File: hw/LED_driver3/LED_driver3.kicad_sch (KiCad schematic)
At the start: 100 parts, among them J1 LED_EN, J10 RJ45_Shielded, J2 I2C, J3 PROG, J4 GPIO, J5 POWER, J6 1WIRE1, J7 1WIRE2, J8 LED, J9 RJ45_Shielded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

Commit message: Routed.
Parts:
- removed TP1, TP2, TP3, TP4: TestPoint, TestPoint:TestPoint_THTPad_D2.0mm_Drill1.0mm, symbol Connector:TestPoint
- added C41: DNP, Capacitor_SMD:C_0603_1608Metric, symbol Device:C
- added R44: 0, Resistor_SMD:R_0603_1608Metric, symbol Device:R
- J5: footprint Connector_Phoenix_MSTB:PhoenixContact_MSTBA_2,5_2-G-5,08_1x02_P5.08mm_Horizontal -> Connector_Phoenix_MSTB:PhoenixContact_MSTB_2,5_2-GF-5,08_1x02_P5.08mm_Horizontal_ThreadedFlange
- R34: value 0.004R -> 6m; LCSC (none) -> C728340
- U5: value INA180 -> INA180A2; LCSC (none) -> C192764
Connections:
- net +3.3V is gone; now on net +3V3: C12.1, C13.1, C16.1, R10.1, U2.4 (VBAT), U2.6 (VDD)
- net SWCLK/BOOT0 is gone; now on net SWCLK: U2.36 (PA14)
- net 12V_SENSE: now also U2.12 (PA1); no longer U2.11 (PA0)
- net CUR_SENSE: now also C41.1, R44.2; no longer U5.1
- net GND: now also C38.2, C39.2, C40.2, C41.2
- net LED_COM: no longer C38.2, C39.2, C40.2
- net O1_SW: now also U2.19 (PB0); no longer U2.17 (PA6)
- net O3_SW: now also U2.17 (PA6); no longer U2.19 (PB0)
- net VCC_SENSE: now also U2.11 (PA0); no longer U2.12 (PA1)
- new net: R44.1, U5.1
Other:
- note added: "TODO: RC článek na sense"

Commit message: Silkscreen finished, bugfixes.
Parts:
- added R45, R46: 330R, Resistor_SMD:R_0603_1608Metric, symbol Device:R
- added R47, R48: 1k5, Resistor_SMD:R_0603_1608Metric, symbol Device:R
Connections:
- net +3V3: now also J2.3 (Pin_3), R47.2, R48.2; no longer J2.4 (Pin_4)
- net 1WIRE: now also U2.30 (PC6)
- net GND: now also J2.4 (Pin_4); no longer J2.3 (Pin_3)
- net SCL: now also R47.1; no longer R12.1, U1.6 (SCL)
- net SDA: now also R48.1; no longer R11.1, U1.5 (SDA)
- net at U2.25 (PB13): no longer R18.1
- net at U2.26 (PB14): now also R18.1; no longer R19.1
- net at U2.27 (PB15): now also R19.1; no longer R20.1
- net at U2.28 (PA8): now also R20.1; no longer R14.1
- net at U2.29 (PA9/NC): now also R14.1
- net at U2.33 (PA11/PA9): now also R45.1
- net at U2.34 (PA12/PA10): now also R46.1
- new net SCL2: R12.1, R45.2, U1.6 (SCL)
- new net SDA2: R11.1, R46.2, U1.5 (SDA)
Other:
- moved on the sheet: R14, R18, R19, R20

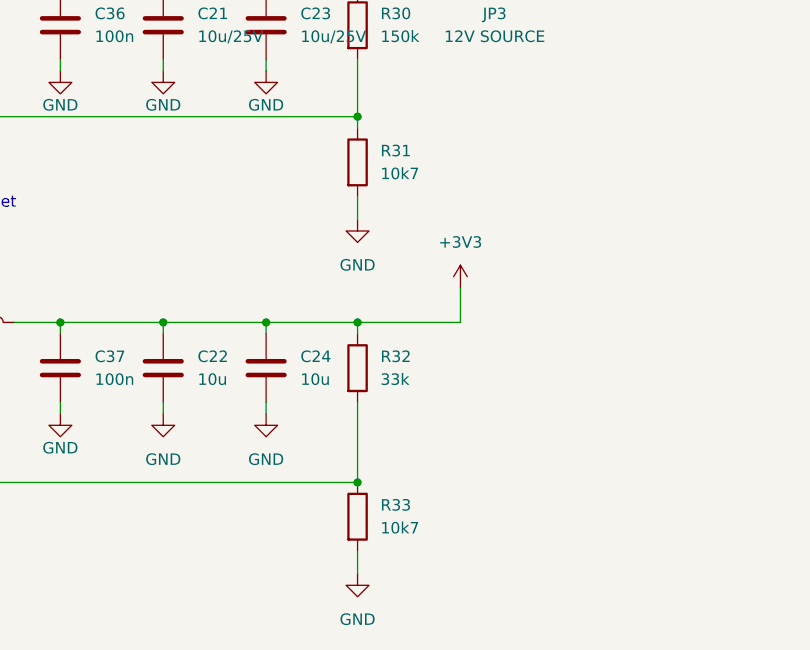
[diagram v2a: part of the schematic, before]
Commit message: Added LCSC numbers.
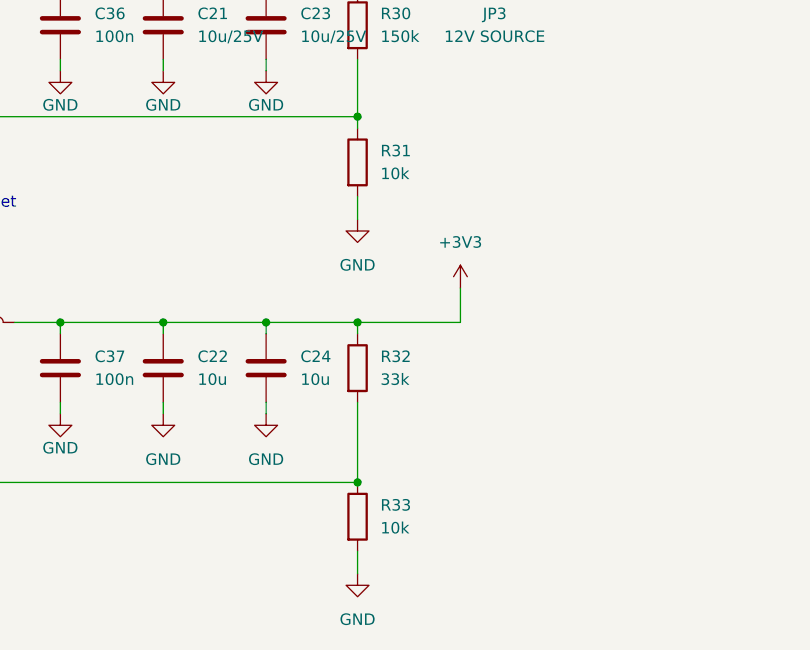
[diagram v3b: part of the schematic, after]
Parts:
- D1: LCSC C72043 -> C2286
- D2, D3, D4, D5, J8: LCSC (none) -> C2286
- R30: LCSC (none) -> C22807
- R31, R33: value 10k7 -> 10k; LCSC (none) -> C25804
- R32: LCSC (none) -> C4216
- R34: LCSC C728340 -> C728340
- R44: LCSC (none) -> C21189
- U1, U5: JLCPCB_CORRECTION (none) -> 0;0;270
- U3, U4: JLCPCB_CORRECTION (none) -> 0;0;270; LCSC (none) -> C5123972
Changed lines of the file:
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@@
 			)
 		)
+		(property "LCSC" "C5123972"
+			(at 193.04 217.17 0)
+			(effects
+				(font
+					(size 1.27 1.27)
+				)
+				(hide yes)
+			)
+		)
+		(property "JLCPCB_CORRECTION" "0;0;270"
+			(at 193.04 217.17 0)
+			(effects
+				(font
+					(size 1.27 1.27)
+				)
+				(hide yes)
+			)
+		)
 		(pin "4"
 		)
@@
 			)
 		)
+		(property "LCSC" "C2286"
+			(at 66.04 114.3 0)
+			(effects
+				(font
+					(size 1.27 1.27)
+				)
+				(hide yes)
+			)
+		)
 		(pin "1"
 		)
@@
 			)
 		)
-		(property "Value" "10k7"
+		(property "Value" "10k"
 			(at 267.97 275.5899 0)
 			(effects
@@
 			)
 		)
+		(property "LCSC" "C25804"
+			(at 265.43 274.32 0)
+			(effects
+				(font
+					(size 1.27 1.27)
+				)
+				(hide yes)
+			)
+		)
 		(pin "1"
 		)
@@
 			)
 		)
+		(property "LCSC" "C2286"
+			(at 45.72 114.3 0)
+			(effects
+				(font
+					(size 1.27 1.27)
+				)
+				(hide yes)
+			)
+		)
 		(pin "1"
 		)
@@
 			)
 		)
+		(property "LCSC" "C21189"
+			(at 354.33 110.49 0)
+			(effects
+				(font
+					(size 1.27 1.27)
+				)
+				(hide yes)
+			)
+		)
 		(pin "1"
 		)
@@
 			)
 		)
-		(property "LCSC" "C72043"
+		(property "LCSC" "C2286"
 			(at 26.67 114.3 90)
 			(effects
@@
 			)
 		)
-		(property "LCSC" "    C728340"
+		(property "LCSC" "C728340"
 			(at 314.96 110.49 0)
 			(effects
@@
 			)
 		)
+		(property "LCSC" "C5123972"
+			(at 193.04 255.27 0)
+			(effects
+				(font
+					(size 1.27 1.27)
+				)
+				(hide yes)
+			)
+		)
+		(property "JLCPCB_CORRECTION" "0;0;270"
+			(at 193.04 255.27 0)
+			(effects
+				(font
+					(size 1.27 1.27)
+				)
+				(hide yes)
+			)
+		)
 		(pin "4"
 		)
@@
 			)
 		)
+		(property "JLCPCB_CORRECTION" "0;0;270"
+			(at 81.28 176.53 0)
+			(effects
+				(font
+					(size 1.27 1.27)
+				)
+				(hide yes)
+			)
+		)
 		(pin "1"
 		)
@@
 			)
 		)
+		(property "LCSC" "C4216"
+			(at 265.43 257.81 0)
+			(effects
+				(font
+					(size 1.27 1.27)
+				)
+				(hide yes)
+			)
+		)
 		(pin "1"
 		)
@@
 			)
 		)
+		(property "LCSC" "C2286"
+			(at 320.04 85.09 0)
+			(effects
+				(font
+					(size 1.27 1.27)
+				)
+				(hide yes)
+			)
+		)
 		(pin "3"
 		)
@@
 			)
 		)
+		(property "LCSC" "C22807"
+			(at 265.43 219.71 0)
+			(effects
+				(font
+					(size 1.27 1.27)
+				)
+				(hide yes)
+			)
+		)
 		(pin "1"
 		)
@@
 			)
 		)
-		(property "Value" "10k7"
+		(property "Value" "10k"
 			(at 267.97 236.2199 0)
 			(effects
@@
 			)
 		)
+		(property "LCSC" "C25804"
+			(at 265.43 234.95 0)
+			(effects
+				(font
+					(size 1.27 1.27)
+				)
+				(hide yes)
+			)
+		)
 		(pin "1"
 		)
@@
 			)
 		)
+		(property "JLCPCB_CORRECTION" "0;0;270"
+			(at 331.47 110.49 0)
+			(effects
+				(font
+					(size 1.27 1.27)
+				)
+				(hide yes)
+			)
+		)
 		(pin "5"
 		)
@@
 			)
 		)
+		(property "LCSC" "C2286"
+			(at 57.15 114.3 0)
+			(effects
+				(font
+					(size 1.27 1.27)
+				)
+				(hide yes)
+			)
+		)
 		(pin "1"
 		)
@@
 			(at 36.83 114.3 0)
 			(effects
+				(font
+					(size 1.27 1.27)
+				)
+				(hide yes)
+			)
+		)
+		(property "LCSC" "C2286"
+			(at 36.83 114.3 0)
+			(effects
